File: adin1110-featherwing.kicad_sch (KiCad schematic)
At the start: 24 parts, among them J2 4039_Header_Male_Vert_16pin_0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, J4 4040_Header_Male_Vert_12pin_0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, SW1 RST, U4 STAT, U5 PWR

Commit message: getting close to schematic completion
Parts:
- added C?: 4063_Capacitor_100n_50V_0402, Shulltronics_Generics:C_0402_HandSolder, symbol Shulltronics_Passives:4063_Capacitor_100n_50V_0402
- added C?: 4062_Capacitor_1nF_2kV_1206, Capacitor_SMD:C_1206_3216Metric_Pad1.33x1.80mm_HandSolder, symbol Shulltronics_Passives:4062_Capacitor_1nF_2kV_1206
- added C?: 4061_Capacitor_470nF_100V_0805, Capacitor_SMD:C_0805_2012Metric_Pad1.18x1.45mm_HandSolder, symbol Shulltronics_Passives:4061_Capacitor_470nF_100V_0805
- added C? (x2): 4059_Cap_220nF_50V_0603, Resistor_SMD:R_0603_1608Metric_Pad0.98x0.95mm_HandSolder, symbol Shulltronics_Passives:4059_Cap_220nF_50V_0603
- added J?: 4060_TerminalBlock_NoScrew, Shulltronics_Connectors:4060_Terminal_Block_0.2in_pitch, symbol Shulltronics_Connectors:4060_TerminalBlock_NoScrew
- added JP?: SPI_CFG1, Jumper:SolderJumper-2_P1.3mm_Open_TrianglePad1.0x1.5mm, symbol Shulltronics_Passives:SolderJumper_2_Open
- added JP?: ~{TX2P4_EN}, Jumper:SolderJumper-2_P1.3mm_Open_TrianglePad1.0x1.5mm, symbol Shulltronics_Passives:SolderJumper_2_Open
- added JP?: ~{MS_SEL}, Jumper:SolderJumper-2_P1.3mm_Open_TrianglePad1.0x1.5mm, symbol Shulltronics_Passives:SolderJumper_2_Open
- added JP?: ~{INT}, Jumper:SolderJumper-2_P1.3mm_Bridged_Pad1.0x1.5mm, symbol Shulltronics_Passives:SolderJumper_2_Bridged
- added JP?: ~{RST}, Jumper:SolderJumper-2_P1.3mm_Bridged_Pad1.0x1.5mm, symbol Shulltronics_Passives:SolderJumper_2_Bridged
- added JP?: ~{SWPD_EN}, Jumper:SolderJumper-2_P1.3mm_Open_TrianglePad1.0x1.5mm, symbol Shulltronics_Passives:SolderJumper_2_Open
- added JP?: ~{CS}, Jumper:SolderJumper-2_P1.3mm_Bridged_Pad1.0x1.5mm, symbol Shulltronics_Passives:SolderJumper_2_Bridged
- added R? (x7): 4064_Resistor_SMD_4k7_0.10W_1%, Shulltronics_Generics:RES-0402, symbol Shulltronics_Passives:4064_Resistor_SMD_4k7_0.10W_1%
- added R?: 4038_Resistor_SMD_100_0.125W_1%, Shulltronics_Generics:RES-0402, symbol Shulltronics_Passives:4038_Resistor_SMD_100_0.125W_1%
- added R?: 4065_Resistor_SMD_1k5_0.10W_1%, Shulltronics_Generics:RES-0402, symbol Shulltronics_Passives:4065_Resistor_SMD_1k5_0.10W_1%
- added SW?: 4012_PushButton_NO_SMD, Shulltronics_ElectroMechanical:4012_PushButton_NO_SMD, symbol Shulltronics_ElectroMechanical:4012_PushButton_NO_SMD
- added TP?: TestPoint, Shulltronics_Generics:TestPoint_Pad_D2.0mm, symbol Shulltronics_Sch_Symbols:TestPoint
- added U?: 4058_TVS_2CH_Super_Speed, Shulltronics_Integrated_Circuits:4058_TVS_2CH_Super_Speed, symbol Shulltronics_Semiconductors:4058_TVS_2CH_Super_Speed
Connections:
- net GND: now also C?.1, C?.1, C?.1, C?.1, C?.1, U?.3
- net MS_SEL: now also JP?.1 (A)
- net VCC: now also C?.2, C?.2, C?.2, R?.1, R?.1, R?.1, R?.1, R?.1
- net ~{CS}: now also JP?.1 (A)
- net ~{RST}: now also U?.5 (~{RST}), JP?.1 (A)
- net ~{INT}: now reaches U?.25 (~{INT})
- net ~{INT}: now also JP?.1 (A)
- net at U?.26 (TEST1): now also R?.2
- net ~{TX2P4_EN}: now reaches U?.31 (~{TX2P4_EN})
- net ~{TX2P4_EN}: now also JP?.1 (A)
- net ~{SWPD_EN}: now reaches U?.33 (~{SWPD_EN})
- net ~{SWPD_EN}: now also JP?.1 (A)
- net SPI_CFG1: now reaches U?.37 (SPI_CFG1)
- net SPI_CFG1: now also JP?.1 (A)
- net at T?.1 (IN+): now also C?.2
- net at T?.2 (IN-): now also C?.2
- net at T?.3 (OUT2A): now also C?.1, R?.1
- net at T?.4 (OUT1B): now also C?.2
- net at T?.5 (PM): now also C?.2
- net at T?.6 (OUT1A): now also J?.1
- net at T?.7 (OUT2B): now also J?.2
- net at R?.1, R?.2: now also U?.5
- net at R?.1, R?.2: now also U?.6
- new net: JP?.2 (B), R?.2 (x4)
- new net: C?.2, R?.2
- new net: C?.1, U?.1
- new net: C?.1, U?.2
- new net ~{CS}_DEF: JP?.2 (B)
- new net ~{INT}_DEF: JP?.2 (B)
- new net ~{RST}_DEF: JP?.2 (B)
- no-connect marks 3 -> 4
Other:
- note added: "D3, D4, D5 (short header, pins 9, 8, 7) are hardwired by Particle Ethernet FW Pin7 also used for CS by Adafruit Ethernet FW"
- moved on the sheet: C?, R8, R9, R?, SW1, T?, U4, U5, U?, Y?

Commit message: sch almost done, started PCB placements
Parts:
- removed R8: 4038_Resistor_SMD_100_0.125W_1%, Shulltronics_Generics:RES-0402, symbol Shulltronics_Passives:4038_Resistor_SMD_100_0.125W_1%
- removed R? (x3): 4064_Resistor_SMD_4k7_0.10W_1%, Shulltronics_Generics:RES-0402, symbol Shulltronics_Passives:4064_Resistor_SMD_4k7_0.10W_1%
- removed R? (x2): 4054_Resistor_SMD_10k2_1/16W_1%, Shulltronics_Generics:RES-0402, symbol Shulltronics_Passives:4054_Resistor_SMD_10k2_1/16W_1%
- removed U5: PWR, Shulltronics_Generics:LED_0402, symbol Shulltronics_Opto:4036_LED_GRN_SMD
- added R1, R2: 4066_Resistor_SMD_10k2_0.1W_1%_0603, Resistor_SMD:R_0603_1608Metric_Pad0.98x0.95mm_HandSolder, symbol Shulltronics_Passives:4066_Resistor_SMD_10k2_0.1W_1%_0603
- added R11, R15, R8: 4064_Resistor_SMD_4k7_0.10W_1%, Shulltronics_Generics:RES-0402, symbol Shulltronics_Passives:4064_Resistor_SMD_4k7_0.10W_1%
- added R17, R9: 4038_Resistor_SMD_100_0.125W_1%, Shulltronics_Generics:RES-0402, symbol Shulltronics_Passives:4038_Resistor_SMD_100_0.125W_1%
- added U3: LED0, Shulltronics_Generics:LED_0402, symbol Shulltronics_Opto:4044_LED_RED_SMD
- added U5: LINK, Shulltronics_Generics:LED_0402, symbol Shulltronics_Opto:4044_LED_RED_SMD
- J3: renamed from J?; footprint Shulltronics_Connectors:4060_Terminal_Block_0.2in_pitch -> Shulltronics_Connectors:4067_SPE_IP20
- T1: renamed from T?; footprint (none) -> Shulltronics_Passives:4057_Super_Tiny_Signal_Transformer
- U4: value STAT -> LED1
- gave numbers to parts that had none: 35
- renumbered J2 to J1, J4 to J2, R9 to R14, SW1 to SW2
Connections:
- net LED_0: now also R8.2, U3.2 (K)
- net LED_1: now also U4.2 (K), R11.2
- net LINK_ST: now also R15.2, U5.2 (K)
- net VCC: now also R14.2, R11.1, R15.1, R17.2, R8.1, R9.2
- net ~{CS}_DEF: now also J1.7
- net ~{INT}_DEF: now also J1.8
- net ~{RST}_DEF: now also J2.10
- net at U4.1 (A): now also R14.1
- net CEXT_3: now reaches C7.2, U1.20 (CEXT_3)
- net TXN: now reaches R4.2, U1.12 (TXN)
- net TXN: now also R1.1
- net RXN: now reaches R5.1, U1.13 (RXN)
- net RXN: now also R2.1
- net RXP: now reaches R6.1, U1.14 (RXP)
- net RXP: now also R1.2
- net TXP: now reaches R7.2, U1.15 (TXP)
- net TXP: now also R2.2
- net CEXT_2: now reaches C8.2, U1.19 (CEXT_2)
- net TEST1: now reaches R3.2, U1.26 (TEST1)
- net XTAL_I: now reaches C4.2, U1.8 (XTAL_I/CLK_IN), Y1.1
- net XTAL_O: now reaches C5.2, U1.9 (XTAL_O), Y1.3
- net D+: now reaches T1.6 (OUT1A)
- net D+: now also J3.2; no longer J3.1
- net D-: now reaches T1.7 (OUT2B)
- net D-: now also J3.1; no longer J3.2
- net at R4.1, R5.2: now also U2.1; no longer U2.5
- net at R6.2, R7.1: now also U2.2; no longer U2.6
- net at U2.1: now also C9.1; no longer C10.1
- net at U2.2: now also C10.1; no longer C9.1
- new net: R9.1, U3.1 (A)
- new net: R17.1, U5.1 (A)
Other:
- moved on the sheet: R14, SW2, U4

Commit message: ready to order
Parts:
- removed SW1: 4012_PushButton_NO_SMD, Shulltronics_ElectroMechanical:4012_PushButton_NO_SMD, symbol Shulltronics_ElectroMechanical:4012_PushButton_NO_SMD
- added C14: 4069_Capacitor_3.3n_50V_0402, Shulltronics_Generics:C_0402_HandSolder, symbol Shulltronics_Passives:4069_Capacitor_3.3n_50V_0402
- added J4: ~, Shulltronics_Connectors:4067_SPE_IP20, symbol Shulltronics_Connectors:4067_SPE_IP20_Right_Angle
- added L1: Shulltronics_Logo, Shulltronics_Generics:Shulltronics_Logo, symbol Shulltronics_Sch_Symbols:Shulltronics_Logo
- added R19: 4065_Resistor_SMD_1k5_0.10W_1%, Shulltronics_Generics:RES-0402, symbol Shulltronics_Passives:4065_Resistor_SMD_1k5_0.10W_1%
- added R20: 4064_Resistor_SMD_4k7_0.10W_1%, Shulltronics_Generics:RES-0402, symbol Shulltronics_Passives:4064_Resistor_SMD_4k7_0.10W_1%
- added R21: 4008_Resistor_SMD_10k_0.125W_1%, Shulltronics_Generics:RES-0402, symbol Shulltronics_Passives:4008_Resistor_SMD_10k_0.125W_1%
- added TP2: LED0, Shulltronics_Generics:TestPoint_Pad_D2.0mm, symbol Shulltronics_Sch_Symbols:TestPoint
- added TP3: LED1, Shulltronics_Generics:TestPoint_Pad_D2.0mm, symbol Shulltronics_Sch_Symbols:TestPoint
- added TP4: LINK, Shulltronics_Generics:TestPoint_Pad_D2.0mm, symbol Shulltronics_Sch_Symbols:TestPoint
- J3: footprint Shulltronics_Connectors:4067_SPE_IP20 -> TerminalBlock:TerminalBlock_bornier-2_P5.08mm
- TP1: value TestPoint -> 1V1
- U1: footprint Package_DFN_QFN:QFN-40-1EP_6x6mm_P0.5mm_EP4.6x4.6mm_ThermalVias -> Shulltronics_Integrated_Circuits:4052_ADIN1110_40QFN
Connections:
- net 1V1: now also TP1.1
- net D+: now also J4.2
- net D-: now also J4.1
- net GND: now also SW2.2, C14.1
- net LED_0: now also TP2.1
- net LED_1: now also TP3.1
- net LINK_ST: now also TP4.1
- net VCC: now also R19.1, R20.2, R21.1
- net ~{CS}: now also R20.1
- net ~{INT}: now also R19.2
- net ~{RST}: now also SW2.1; no longer JP2.1 (A), U1.5 (~{RST})
- net USER: now reaches J1.1
- net A2: now reaches J1.10
- net A1: now reaches J1.11
- net A0: now reaches J1.12
- net A3: now reaches J1.9
- net Da+: now reaches C9.2, T1.1 (IN+)
- net Da-: now reaches C10.2, T1.2 (IN-)
- net Dc+: now reaches R4.1, R5.2
- net Dc+: now also U2.6; no longer U2.1
- net D13: now reaches J2.4
- net D12: now reaches J2.5
- net D11: now reaches J2.6
- net D10: now reaches J2.7
- net D9: now reaches J2.8
- net D6: now reaches J2.9
- net Dc-: now reaches R6.2, R7.1
- net Dc-: now also U2.5; no longer U2.2
- net Db+: now reaches C9.1, U2.1
- net Db-: now reaches C10.1, U2.2
- net RXN renamed RX-
- net RXP renamed RX+
- net TXN renamed TX-
- net TXP renamed TX+
- new net: C14.2, J4.3
- new net ~{RESET}: JP2.1 (A), R21.2, U1.5 (~{RST})
- no-connect marks 4 -> 21
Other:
- company: (none) -> Shulltronics
- title: (none) -> ADIN1110 FeatherWing
- moved on the sheet: C10, C9, J3, SW2, TP1

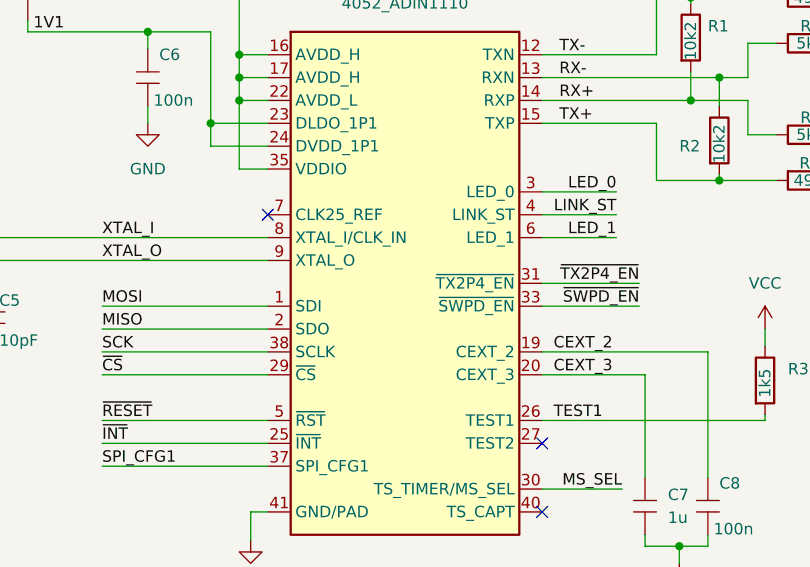
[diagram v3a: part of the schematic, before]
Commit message: created BOM for DigiKey order
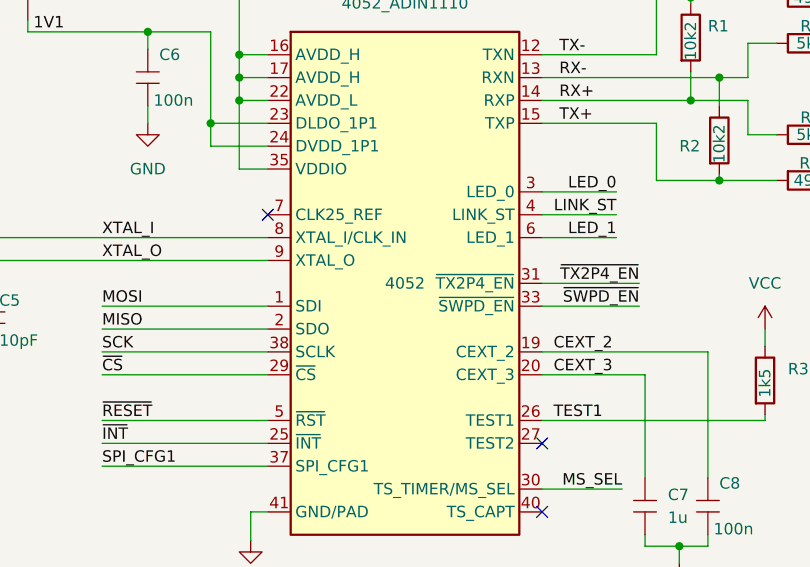
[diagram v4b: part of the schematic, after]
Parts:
- U1: SPN (none) -> 4052
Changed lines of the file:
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@@
       (effects (font (size 1.27 1.27)) hide)
+    )
+    (property "SPN" "4052" (at 113.665 60.325 0)
+      (effects (font (size 1.27 1.27)))
     )
     (pin "1")
